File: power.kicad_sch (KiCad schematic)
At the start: 7 parts, among them J2 HTSW-102-07-G-S, U1 TPSM861253RDXR

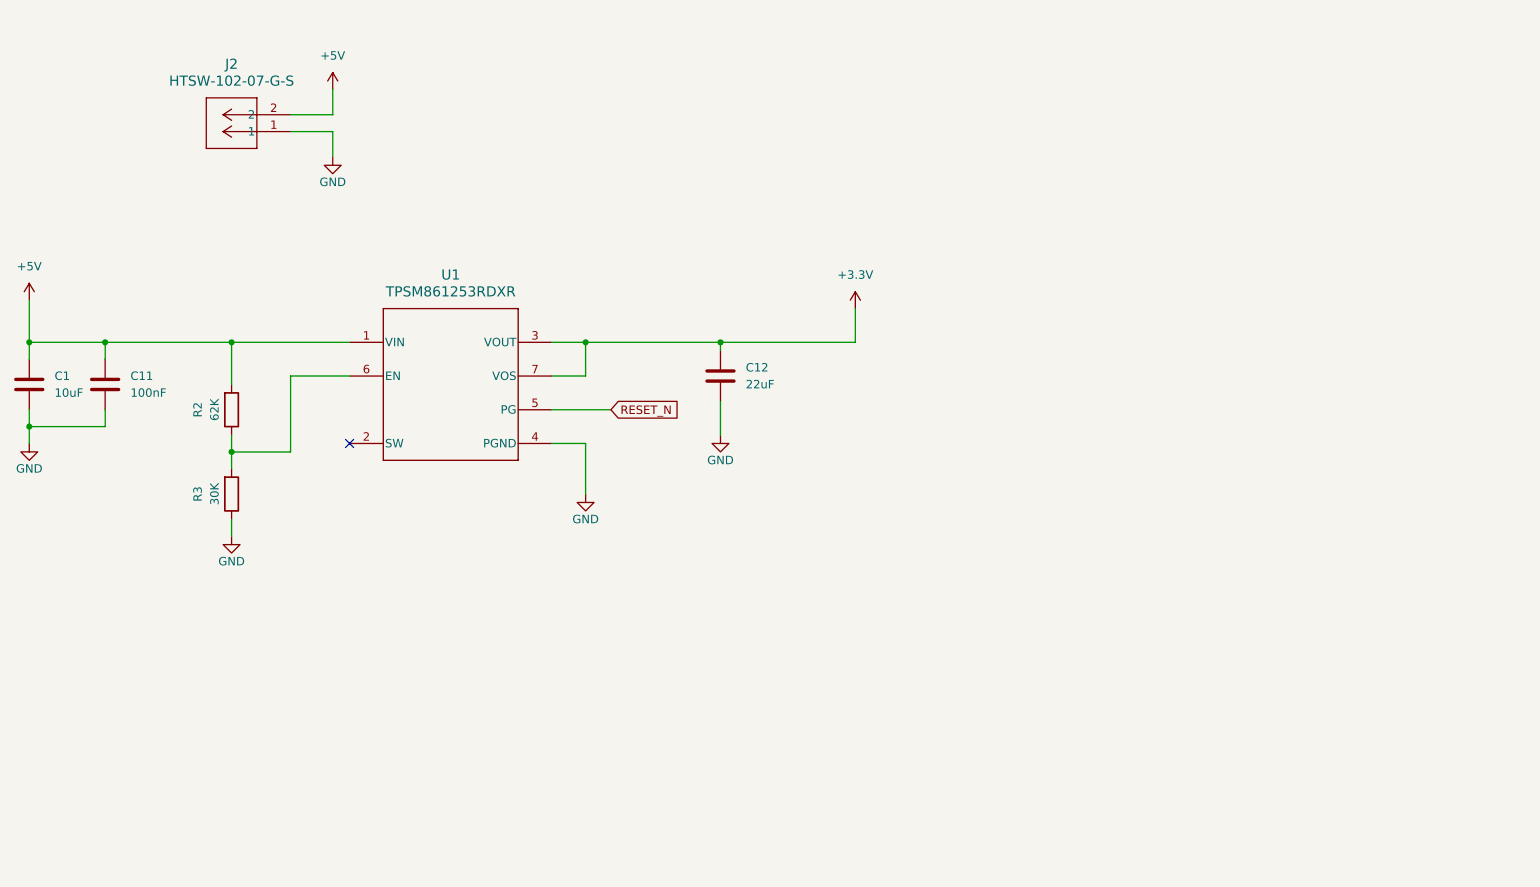
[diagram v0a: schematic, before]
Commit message: More cleanups and add some test points
Signed-off-by: Corey Minyard <corey@minyard.net>
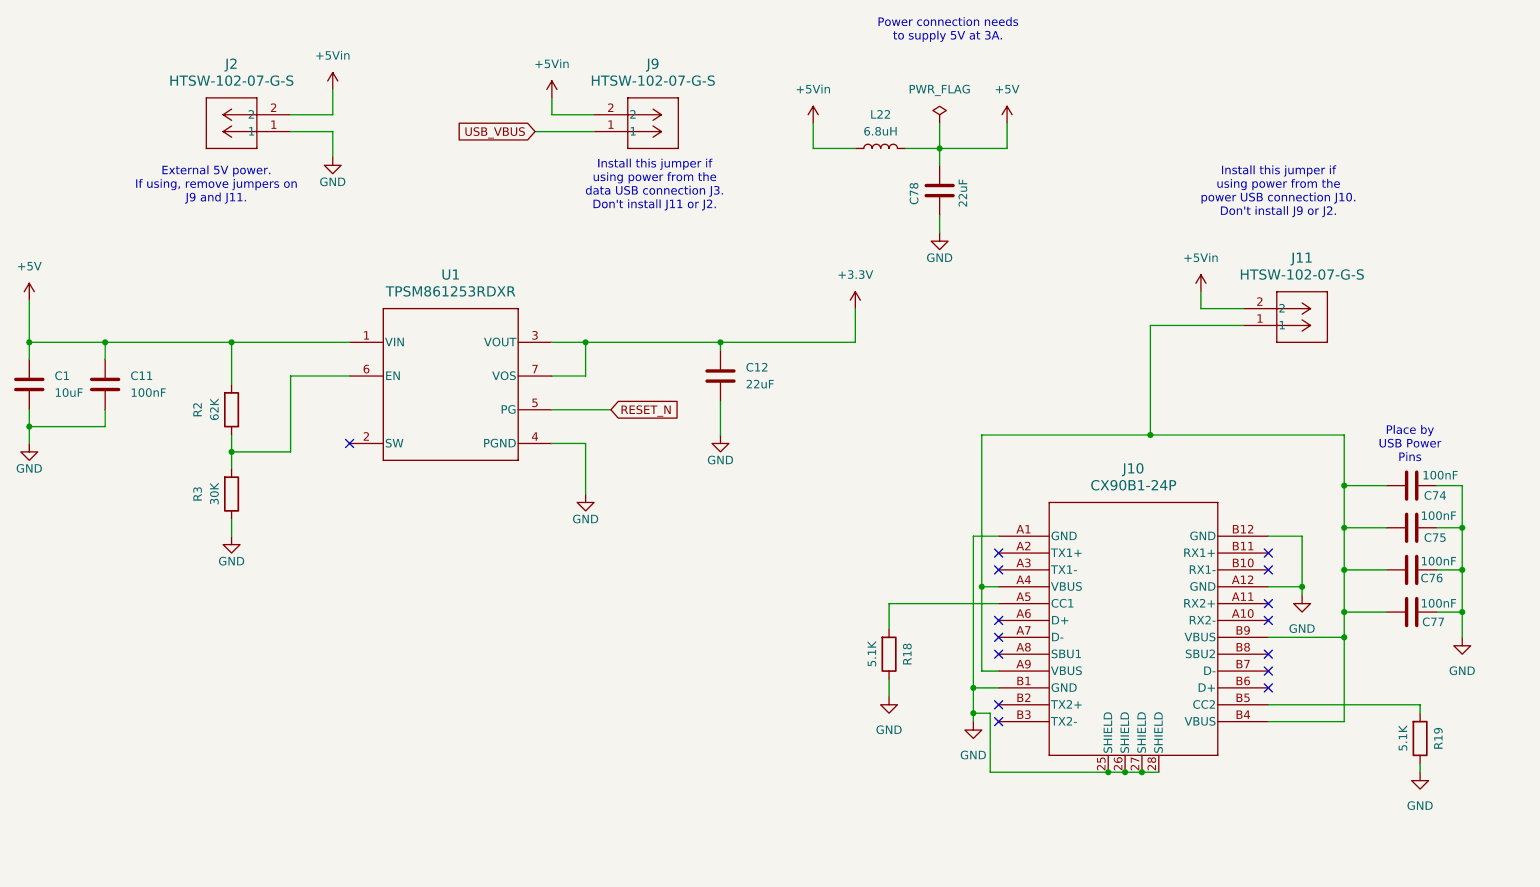
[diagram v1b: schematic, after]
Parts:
- added C74, C75, C76, C77: 100nF, Capacitor_SMD:C_0402_1005Metric, symbol Device:C
- added C78: 22uF, Capacitor_SMD:C_1206_3216Metric_Pad1.33x1.80mm_HandSolder, symbol Device:C
- added J10: CX90B1-24P, footprints:CX90B1-24P_HIR, symbol Local Connectors:CX90B1-24P
- added J11, J9: HTSW-102-07-G-S, footprints:CON2_1X2_TU_TSW, symbol Local Connectors:HTSW-102-07-G-S_1
- added L22: 6.8uH, Inductor_SMD:L_1210_3225Metric_Pad1.42x2.65mm_HandSolder, symbol Device:L
- added R18, R19: 5.1K, Resistor_SMD:R_0402_1005Metric, symbol Device:R
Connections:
- net +5V: now also C78.2, L22.2; no longer J2.2
- net GND: now also C74.2, C75.2, C76.2, C77.2, C78.1, J10.25 (SHIELD), J10.26 (SHIELD), J10.27 (SHIELD), J10.28 (SHIELD), J10.A1 (GND), J10.A12 (GND), J10.B1 (GND), J10.B12 (GND), R18.1, R19.1
- new net: J10.A5 (CC1), R18.2
- new net: C74.1, C75.1, C76.1, C77.1, J10.A4 (VBUS), J10.A9 (VBUS), J10.B4 (VBUS), J10.B9 (VBUS), J11.1
- new net: J10.B5 (CC2), R19.2
- new net +5Vin: J11.2, J2.2, J9.2, L22.1
- new net USB_VBUS: J9.1
- no-connect marks 1 -> 15
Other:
- note added: "External 5V power. If using, remove jumpers on J9 and J11."
- note added: "Install this jumper if using power from the data USB connection J3. Don't install J11 or J2."
- note added: "Install this jumper if using power from the power USB connection J10. Don't install J9 or J2."
- note added: "Place by USB Power Pins"
- note added: "Power connection needs to supply 5V at 3A."

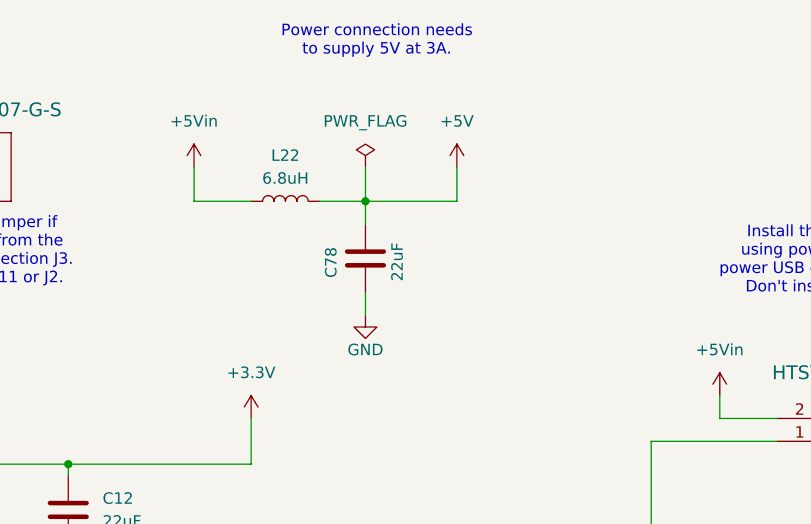
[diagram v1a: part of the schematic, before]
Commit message: Start working on BOM, fix supply indoctors
Signed-off-by: Corey Minyard <corey@minyard.net>
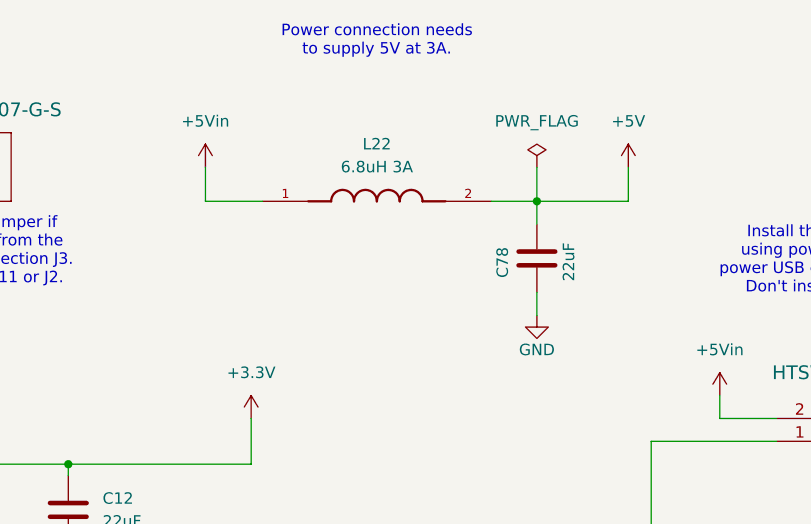
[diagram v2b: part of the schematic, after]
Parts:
- L22: value 6.8uH -> 6.8uH 3A; footprint Inductor_SMD:L_1210_3225Metric_Pad1.42x2.65mm_HandSolder -> footprints:IND_1255AY-6R8M=P3; symbol Device:L -> Local Passives:1255AY-6R8M=P3; Check_prices (none) -> https://www.snapeda.com/parts/1255AY-6R8M=P3/Murata/view-pa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; Description_1 (none) -> Inductor with Inductance: 6.8uH Tol. +/-20%, Package: 2424 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; DigiKey_Part_Number (none) -> 490-14063-1-ND; MANUFACTURER (none) -> Murata; MAXIMUM_PACKAGE_HEIGHT (none) -> 4.5mm; MF (none) -> Murata; MP (none) -> 1255AY-6R8M=P3; PARTREV (none) -> N/A; Package (none) -> NONSTANDARD; STANDARD (none) -> Manufacturer Recommendations; SnapEDA_Link (none) -> https://www.snapeda.com/parts/1255AY-6R8M=P3/Murata/view-pa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
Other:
- moved on the sheet: C78
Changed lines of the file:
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@@
 	)
 	(junction
-		(at 171.45 38.1)
+		(at 190.5 38.1)
 		(diameter 0)
 		(color 0 0 0 0)
@@
 	(wire
 		(pts
-			(xy 171.45 38.1) (xy 171.45 40.64)
+			(xy 190.5 38.1) (xy 190.5 40.64)
 		)
 		(stroke
@@
 	(wire
 		(pts
-			(xy 171.45 34.29) (xy 171.45 38.1)
+			(xy 190.5 34.29) (xy 190.5 38.1)
 		)
 		(stroke
@@
 	(wire
 		(pts
-			(xy 171.45 38.1) (xy 181.61 38.1)
+			(xy 190.5 38.1) (xy 200.66 38.1)
 		)
 		(stroke
@@
 	(wire
 		(pts
-			(xy 171.45 48.26) (xy 171.45 50.8)
+			(xy 190.5 48.26) (xy 190.5 50.8)
 		)
 		(stroke
@@
 	(wire
 		(pts
-			(xy 166.37 38.1) (xy 171.45 38.1)
+			(xy 185.42 38.1) (xy 190.5 38.1)
 		)
 		(stroke
@@
 	(wire
 		(pts
-			(xy 152.4 38.1) (xy 158.75 38.1)
+			(xy 153.67 38.1) (xy 160.02 38.1)
 		)
 		(stroke
@@
 	(wire
 		(pts
-			(xy 181.61 38.1) (xy 181.61 34.29)
+			(xy 200.66 38.1) (xy 200.66 34.29)
 		)
 		(stroke
@@
 	(wire
 		(pts
-			(xy 152.4 34.29) (xy 152.4 38.1)
+			(xy 153.67 34.29) (xy 153.67 38.1)
 		)
 		(stroke
@@
 	(symbol
 		(lib_id "Device:C")
-		(at 171.45 44.45 180)
+		(at 190.5 44.45 180)
 		(unit 1)
 		(exclude_from_sim no)
@@
 		(dnp no)
 		(property "Reference" "C78"
-			(at 167.64 43.18 90)
+			(at 186.69 43.18 90)
 			(effects
 				(font
@@
 		)
 		(property "Value" "22uF"
-			(at 175.006 42.672 90)
+			(at 194.056 42.672 90)
 			(effects
 				(font
@@
 		)
 		(property "Footprint" "Capacitor_SMD:C_1206_3216Metric_Pad1.33x1.80mm_HandSolder"
-			(at 170.4848 40.64 0)
+			(at 189.5348 40.64 0)
 			(effects
 				(font
@@
 		)
 		(property "Datasheet" "~"
-			(at 171.45 44.45 0)
+			(at 190.5 44.45 0)
 			(effects
 				(font
@@
 		)
 		(property "Description" "Unpolarized capacitor"
-			(at 171.45 44.45 0)
+			(at 190.5 44.45 0)
 			(effects
 				(font
@@
 	(symbol
 		(lib_id "power:+12V")
-		(at 181.61 34.29 0)
+		(at 200.66 34.29 0)
 		(unit 1)
 		(exclude_from_sim no)
@@
 		(fields_autoplaced yes)
 		(property "Reference" "#PWR083"
-			(at 181.61 38.1 0)
+			(at 200.66 38.1 0)
 			(effects
 				(font
@@
 		)
 		(property "Value" "+5V"
-			(at 181.61 29.21 0)
+			(at 200.66 29.21 0)
 			(effects
 				(font
@@
 		)
 		(property "Footprint" ""
-			(at 181.61 34.29 0)
+			(at 200.66 34.29 0)
 			(effects
 				(font
@@
 		)
 		(property "Datasheet" ""
-			(at 181.61 34.29 0)
+			(at 200.66 34.29 0)
 			(effects
 				(font
@@
 		)
 		(property "Description" "Power symbol creates a global label with name \"+12V\""
-			(at 181.61 34.29 0)
+			(at 200.66 34.29 0)
 			(effects
 				(font
@@
 	)
 	(symbol
-		(lib_id "Device:L")
-		(at 162.56 38.1 90)
+		(lib_id "Local Passives:1255AY-6R8M=P3")
+		(at 172.72 38.1 0)
 		(unit 1)
 		(exclude_from_sim no)
@@
 		(fields_autoplaced yes)
 		(property "Reference" "L22"
-			(at 162.56 33.02 90)
+			(at 172.72 31.75 0)
 			(effects
 				(font
@@
 			)
 		)
-		(property "Value" "6.8uH"
-			(at 162.56 35.56 90)
+		(property "Value" "6.8uH 3A"
+			(at 172.72 34.29 0)
 			(effects
 				(font
@@
 			)
 		)
-		(property "Footprint" "Inductor_SMD:L_1210_3225Metric_Pad1.42x2.65mm_HandSolder"
-			(at 162.56 38.1 0)
+		(property "Footprint" "footprints:IND_1255AY-6R8M=P3"
+			(at 172.72 47.498 0)
 			(effects
 				(font
 					(size 1.27 1.27)
 				)
+				(justify bottom)
 				(hide yes)
 			)
 		)
 		(property "Datasheet" "~"
-			(at 162.56 38.1 0)
+			(at 172.72 38.1 0)
 			(effects
 				(font
@@
 		)
 		(property "Description" "Inductor"
-			(at 162.56 38.1 0)
+			(at 172.72 38.1 0)
 			(effects
 				(font
@@
 			)
 		)
+		(property "DigiKey_Part_Number" "490-14063-1-ND"
+			(at 173.482 53.086 0)
+			(effects
+				(font
+					(size 1.27 1.27)
+				)
+				(justify bottom)
+				(hide yes)
+			)
+		)
+		(property "SnapEDA_Link" "https://www.snapeda.com/parts/1255AY-6R8M=P3/Murata/view-part/?ref=snap"
+			(at 174.498 43.942 0)
+			(effects
+				(font
+					(size 1.27 1.27)
+				)
+				(justify bottom)
+				(hide yes)
+			)
+		)
+		(property "MAXIMUM_PACKAGE_HEIGHT" "4.5mm"
+			(at 156.972 53.594 0)
+			(effects
+				(font
+					(size 1.27 1.27)
+				)
+				(justify bottom)
+				(hide yes)
+			)
+		)
+		(property "Package" "NONSTANDARD"
+			(at 173.482 58.166 0)
+			(effects
+				(font
+					(size 1.27 1.27)
+				)
+				(justify bottom)
+				(hide yes)
+			)
+		)
+		(property "Check_prices" "https://www.snapeda.com/parts/1255AY-6R8M=P3/Murata/view-part/?ref=eda"
+			(at 172.974 40.64 0)
+			(effects
+				(font
+					(size 1.27 1.27)
+				)
+				(justify bottom)
+				(hide yes)
+			)
+		)
+		(property "STANDARD" "Manufacturer Recommendations"
+			(at 172.466 50.546 0)
+			(effects
+				(font
+					(size 1.27 1.27)
+				)
+				(justify bottom)
+				(hide yes)
+			)
+		)
+		(property "PARTREV" "N/A"
+			(at 192.024 52.578 0)
+			(effects
+				(font
+					(size 1.27 1.27)
+				)
+				(justify bottom)
+				(hide yes)
+			)
+		)
+		(property "MF" "Murata"
+			(at 188.468 55.118 0)
+			(effects
+				(font
+					(size 1.27 1.27)
+				)
+				(justify bottom)
+				(hide yes)
+			)
+		)
+		(property "MP" "1255AY-6R8M=P3"
+			(at 172.974 55.626 0)
+			(effects
+				(font
+					(size 1.27 1.27)
+				)
+				(justify bottom)
+				(hide yes)
+			)
+		)
+		(property "Description_1" "Inductor with Inductance: 6.8uH Tol. +/-20%, Package: 2424 (6060)"
+			(at 172.212 34.798 0)
+			(effects
+				(font
+					(size 1.27 1.27)
+				)
+				(justify bottom)
+				(hide yes)
+			)
+		)
+		(property "MANUFACTURER" "Murata"
+			(at 187.198 57.658 0)
+			(effects
+				(font
+					(size 1.27 1.27)
+				)
+				(justify bottom)
+				(hide yes)
+			)
+		)
 		(pin "1"
 		)
@@
 	(symbol
 		(lib_id "power:+12V")
-		(at 152.4 34.29 0)
+		(at 153.67 34.29 0)
 		(unit 1)
 		(exclude_from_sim no)
@@
 		(fields_autoplaced yes)
 		(property "Reference" "#PWR084"
-			(at 152.4 38.1 0)
+			(at 153.67 38.1 0)
 			(effects
 				(font
@@
 		)
 		(property "Value" "+5Vin"
-			(at 152.4 29.21 0)
+			(at 153.67 29.21 0)
 			(effects
 				(font
@@
 		)
 		(property "Footprint" ""
-			(at 152.4 34.29 0)
+			(at 153.67 34.29 0)
 			(effects
 				(font
@@
 		)
 		(property "Datasheet" ""
-			(at 152.4 34.29 0)
+			(at 153.67 34.29 0)
 			(effects
 				(font
@@
 		)
 		(property "Description" "Power symbol creates a global label with name \"+12V\""
-			(at 152.4 34.29 0)
+			(at 153.67 34.29 0)
 			(effects
 				(font
@@
 	(symbol
 		(lib_id "power:GND")
-		(at 171.45 50.8 0)
+		(at 190.5 50.8 0)
 		(unit 1)
 		(exclude_from_sim no)
@@
 		(dnp no)
 		(property "Reference" "#PWR085"
-			(at 171.45 57.15 0)
+			(at 190.5 57.15 0)
 			(effects
 				(font
@@
 		)
 		(property "Value" "GND"
-			(at 171.45 54.61 0)
+			(at 190.5 54.61 0)
 			(effects
 				(font
@@
 		)
 		(property "Footprint" ""
-			(at 171.45 50.8 0)
+			(at 190.5 50.8 0)
 			(effects
 				(font
@@
 		)
 		(property "Datasheet" ""
-			(at 171.45 50.8 0)
+			(at 190.5 50.8 0)
 			(effects
 				(font
@@
 		)
 		(property "Description" "Power symbol creates a global label with name \"GND\" , ground"
-			(at 171.45 50.8 0)
+			(at 190.5 50.8 0)
 			(effects
 				(font
@@
 	(symbol
 		(lib_id "power:PWR_FLAG")
-		(at 171.45 34.29 0)
+		(at 190.5 34.29 0)
 		(unit 1)
 		(exclude_from_sim no)
@@
 		(fields_autoplaced yes)
 		(property "Reference" "#FLG04"
-			(at 171.45 32.385 0)
+			(at 190.5 32.385 0)
 			(effects
 				(font
@@
 		)
 		(property "Value" "PWR_FLAG"
-			(at 171.45 29.21 0)
+			(at 190.5 29.21 0)
 			(effects
 				(font
@@
 		)
 		(property "Footprint" ""
-			(at 171.45 34.29 0)
+			(at 190.5 34.29 0)
 			(effects
 				(font
@@
 		)
 		(property "Datasheet" "~"
-			(at 171.45 34.29 0)
+			(at 190.5 34.29 0)
 			(effects
 				(font
@@
 		)
 		(property "Description" "Special symbol for telling ERC where power comes from"
-			(at 171.45 34.29 0)
+			(at 190.5 34.29 0)
 			(effects
 				(font
